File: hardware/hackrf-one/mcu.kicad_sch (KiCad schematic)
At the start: 134 parts, among them J1 USB-MICRO-B, P20 GPIO, P22 I2S, P23 DBGEN, P24 TRST, P25 LPC_ISP, P26 LPC_JTAG, P28 SD, P29 CPLD_JTAG, P3 GND, P30 BANK2_AUX, P5 LEDS, P68 SPIFI_CS, P69 VREGMODE, P70 EN_1V8, P71 ID, P72 GP_CLKIN, P73 P1_2, P74 P1_1, P75 GP_CLKIN, P76 GP_CLKIN, P77 GP_CLKIN, P78 GP_CLKIN, P79 GP_CLKIN, P80 SHIELD, P81 SPIFI_SIO2, P82 SPIFI_SIO3, Q5 MOSFET_P, SW1 DFU, SW2 RESET, U15 TVS, U20 W25Q80, U21 TPS62410, U23 LPC4320FBD144, U24 GSG-XC2C64A-7VQG100C, X2 MCU_XTAL, X3 RTC_XTAL

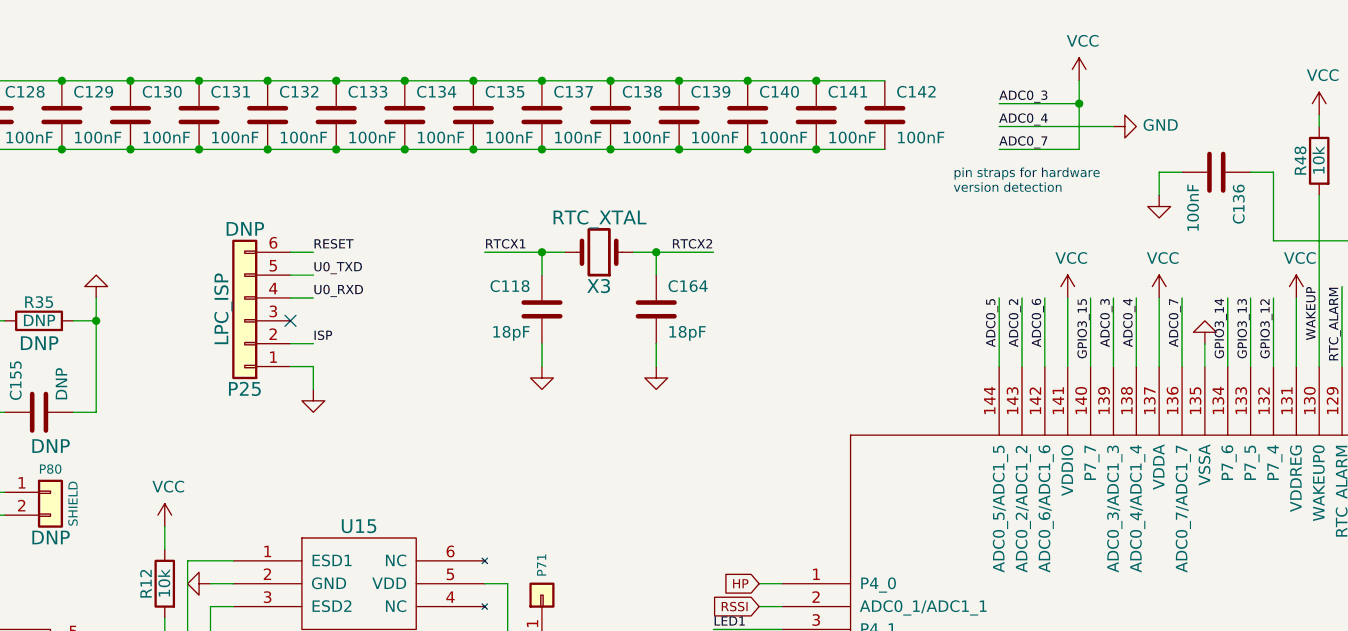
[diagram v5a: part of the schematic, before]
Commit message: HackRF One: update version detection pin straps
Hardware version detection now requires sensing of an analog voltage.
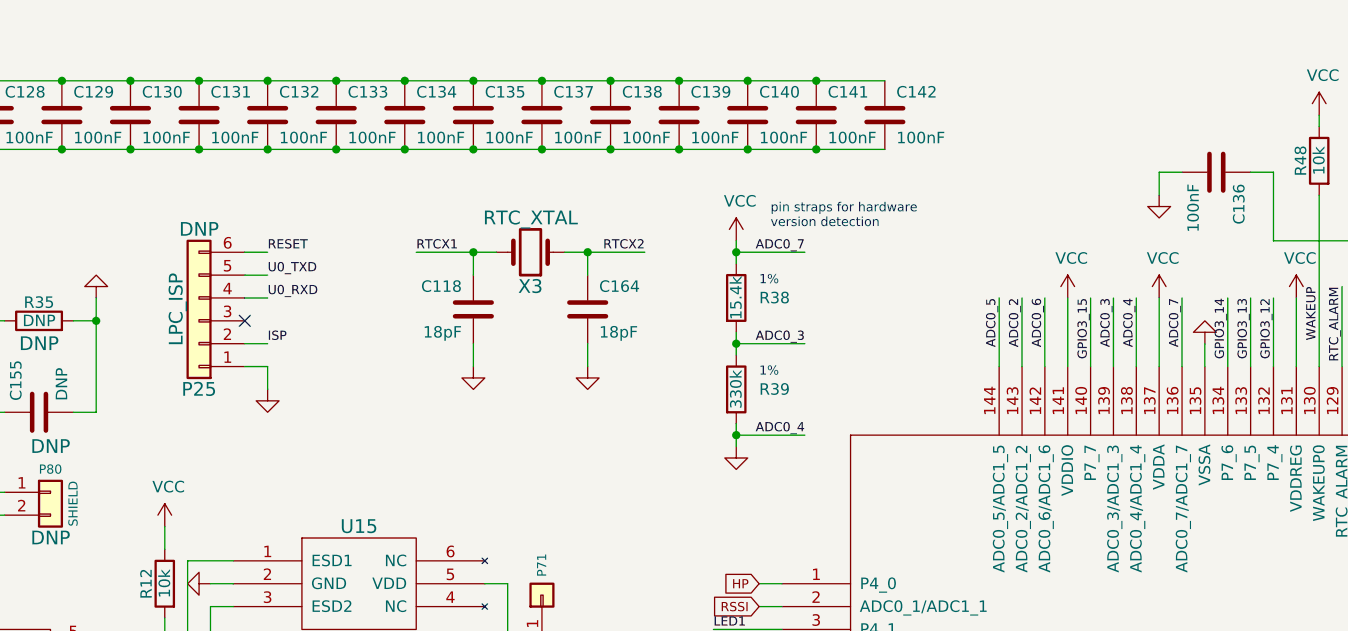
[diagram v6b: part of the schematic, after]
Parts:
- added R38: 15.4k, hackrf:GSG-0402, symbol Device:R
- added R39: 330k, hackrf:GSG-0402, symbol Device:R
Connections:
- net GND: now also R39.2
- net VCC: now also R38.1; no longer U23.139 (ADC0_3/ADC1_3)
- new net ADC0_3: R38.2, R39.1, U23.139 (ADC0_3/ADC1_3)
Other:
- moved on the sheet: C118, C164, P25, X3

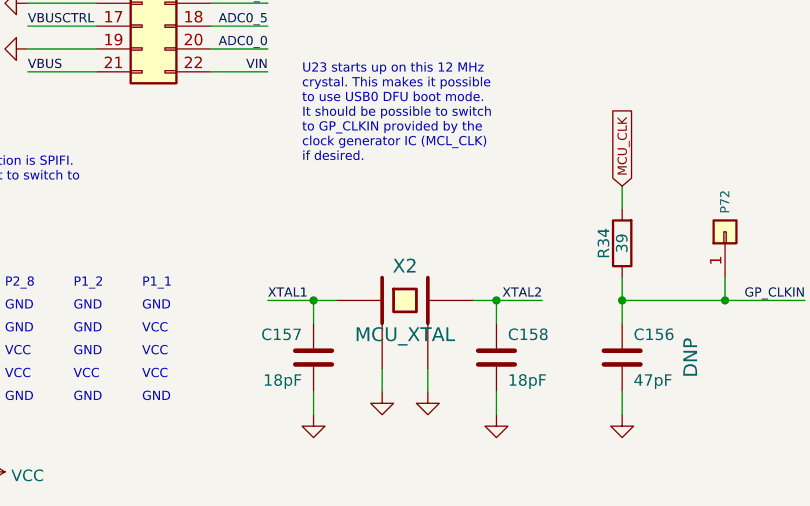
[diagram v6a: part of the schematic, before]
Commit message: HackRF One: clean up symbol value names
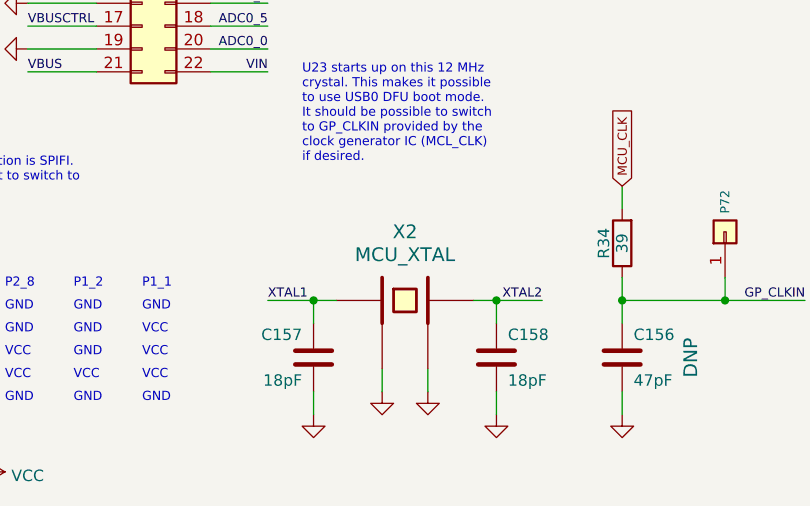
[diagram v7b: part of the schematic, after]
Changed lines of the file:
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@@
   (symbol (lib_id "hackrf:GSG-XTAL4PIN") (at 116.84 245.11 0) (unit 1)
     (in_bom yes) (on_board yes)
-    (property "Reference" "X2" (id 0) (at 116.84 241.3 0)
+    (property "Reference" "X2" (id 0) (at 116.84 237.49 0)
       (effects (font (size 1.524 1.524)))
     )
-    (property "Value" "MCU_XTAL" (id 1) (at 116.84 248.92 0)
+    (property "Value" "MCU_XTAL" (id 1) (at 116.84 240.03 0)
       (effects (font (size 1.524 1.524)))
     )

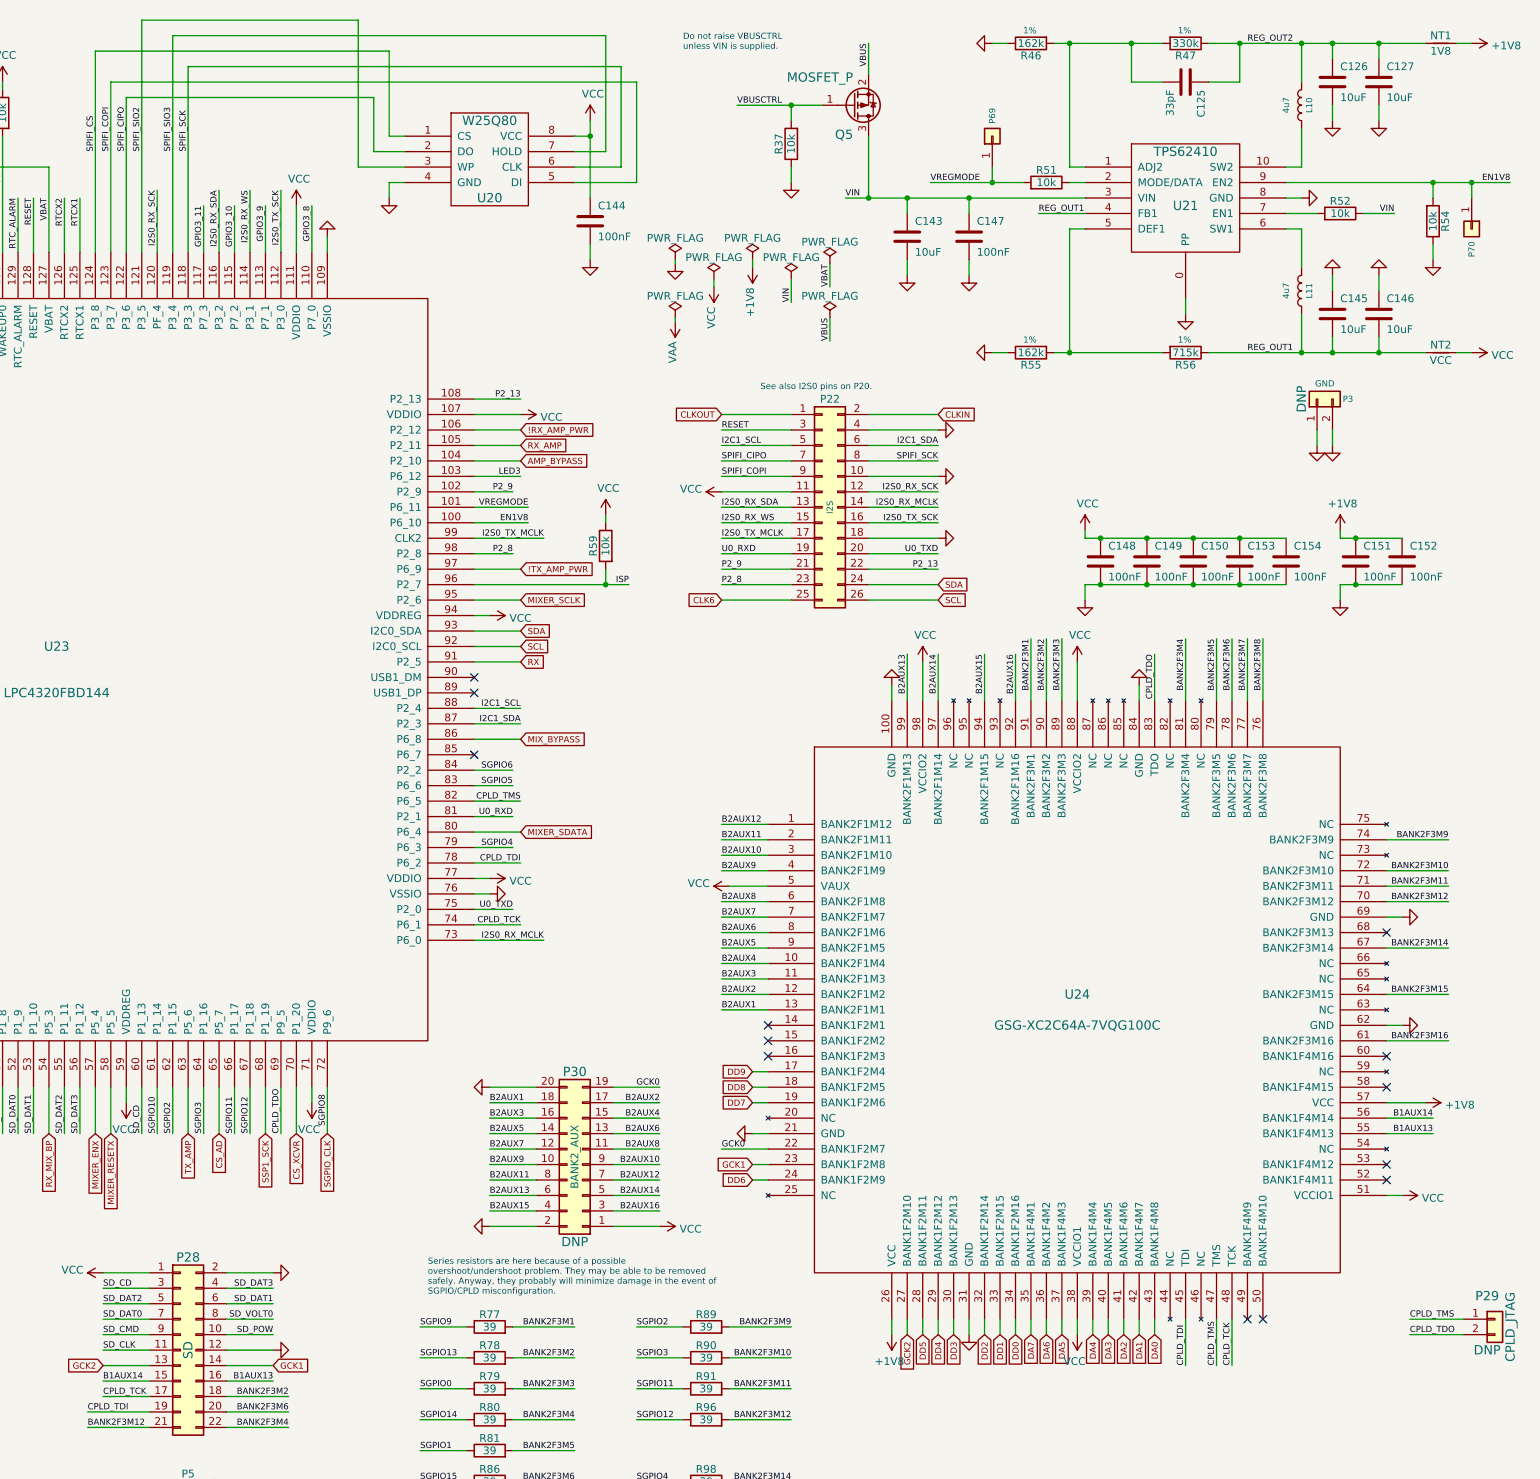
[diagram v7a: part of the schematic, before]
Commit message: HackRF One: correct fabrication attributes and DNP
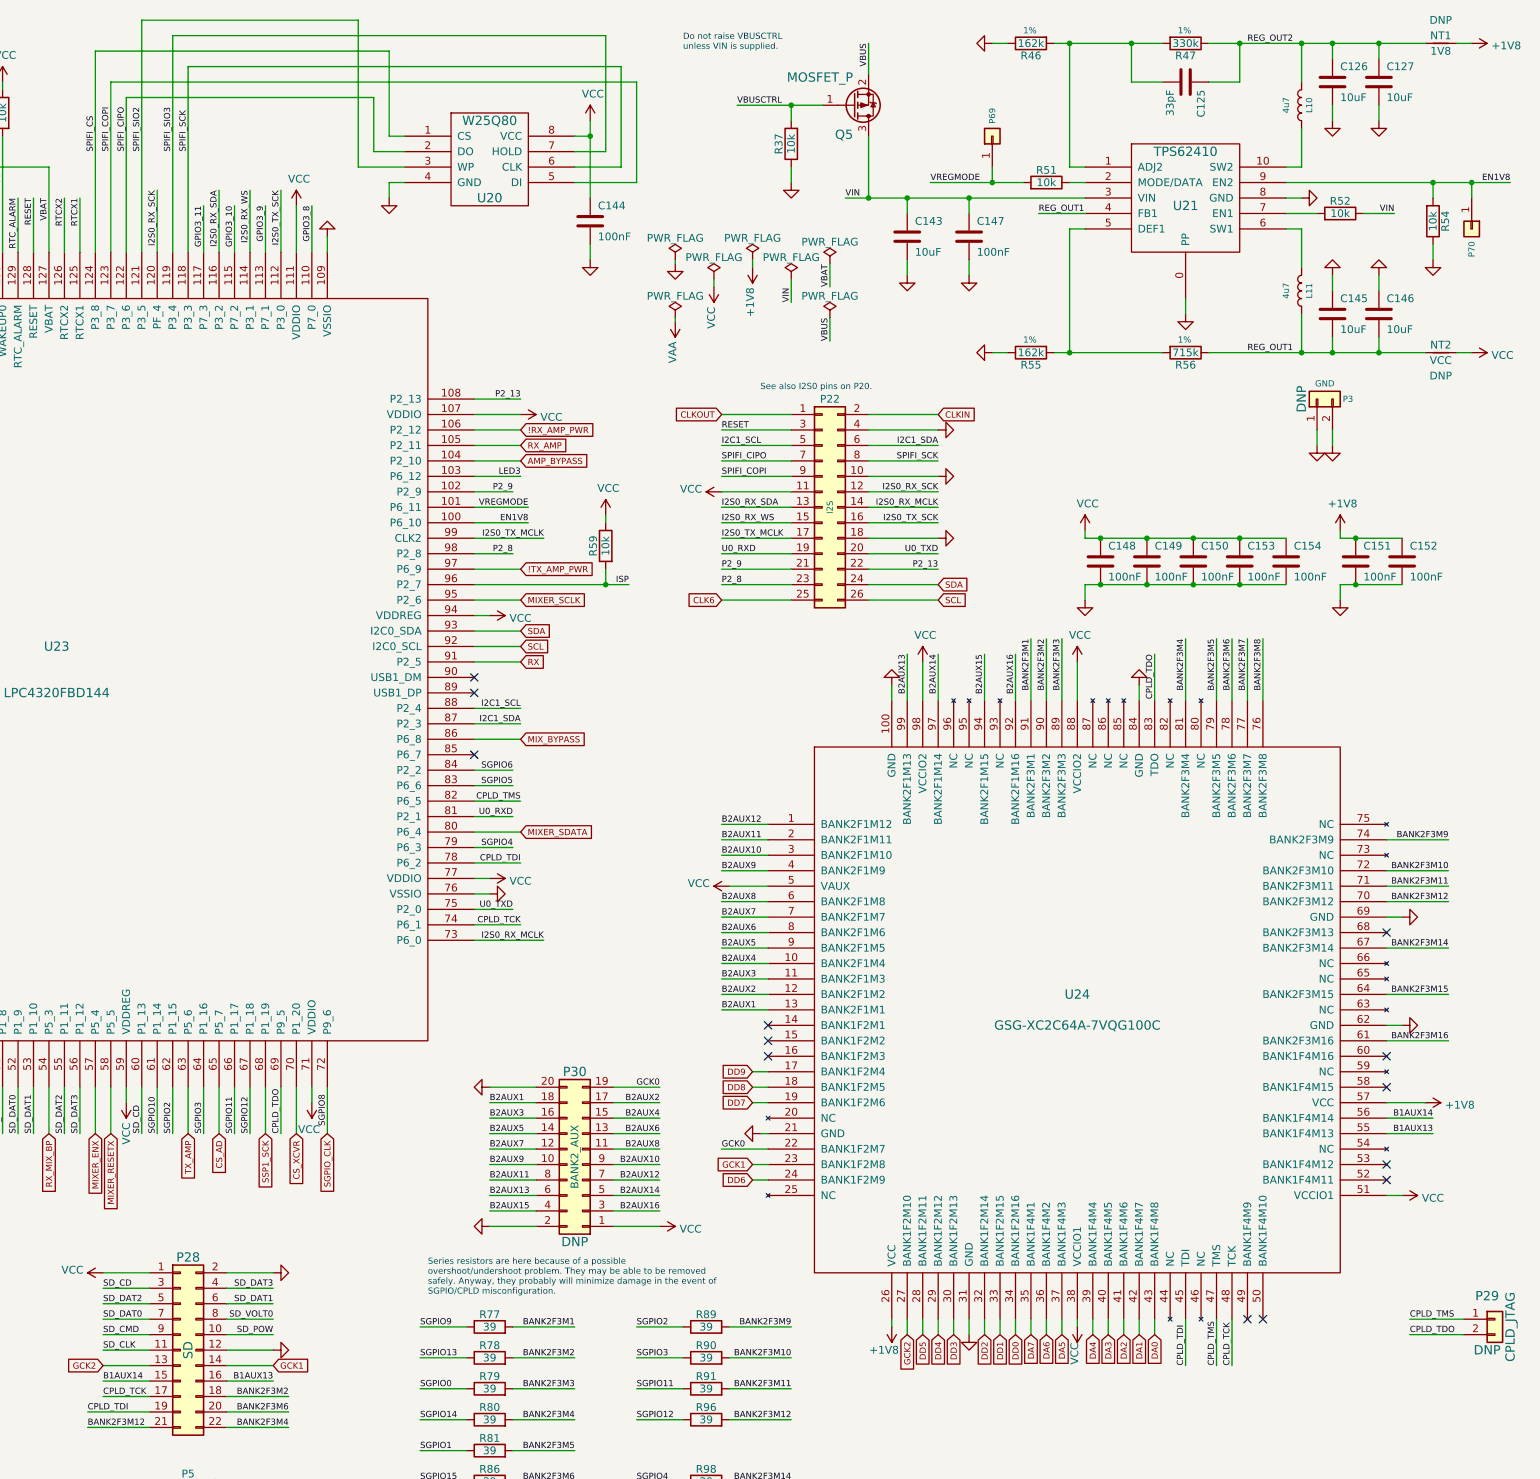
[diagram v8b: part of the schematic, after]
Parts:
- P23, P24, P68, P69, P70, P71, P72, P73, P74, P81, P82: DNP DNP -> (none); now left out of the parts list
- P75: value GP_CLKIN -> SGPIO0; DNP DNP -> (none); now left out of the parts list
- P76: value GP_CLKIN -> SGPIO7; DNP DNP -> (none); now left out of the parts list
- P77: value GP_CLKIN -> SGPIO9; DNP DNP -> (none); now left out of the parts list
- P78: value GP_CLKIN -> SGPIO10; DNP DNP -> (none); now left out of the parts list
- P79: value GP_CLKIN -> SGPIO11; DNP DNP -> (none); now left out of the parts list
